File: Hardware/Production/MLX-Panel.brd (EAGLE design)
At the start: 62 x 62 mm, 135 parts, among them U1 MLX90393_MAGNETOMETER, U2 MLX90393_MAGNETOMETER, U3 MLX90393_MAGNETOMETER, U4 MLX90393_MAGNETOMETER, U5 MLX90393_MAGNETOMETER, U6 MLX90393_MAGNETOMETER, U7 MLX90393_MAGNETOMETER, U8 MLX90393_MAGNETOMETER, U9 MLX90393_MAGNETOMETER

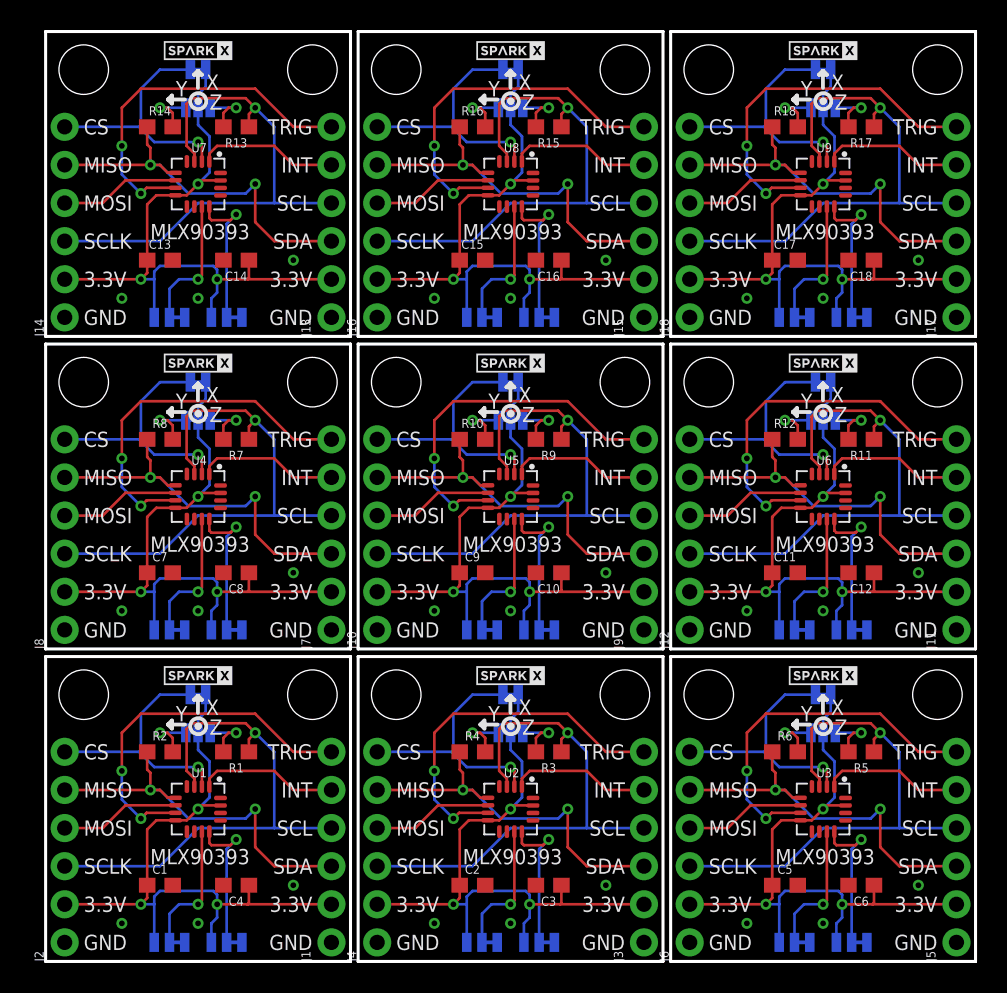
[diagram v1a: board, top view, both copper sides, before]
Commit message: fixed panel with tstop, pushed berbers
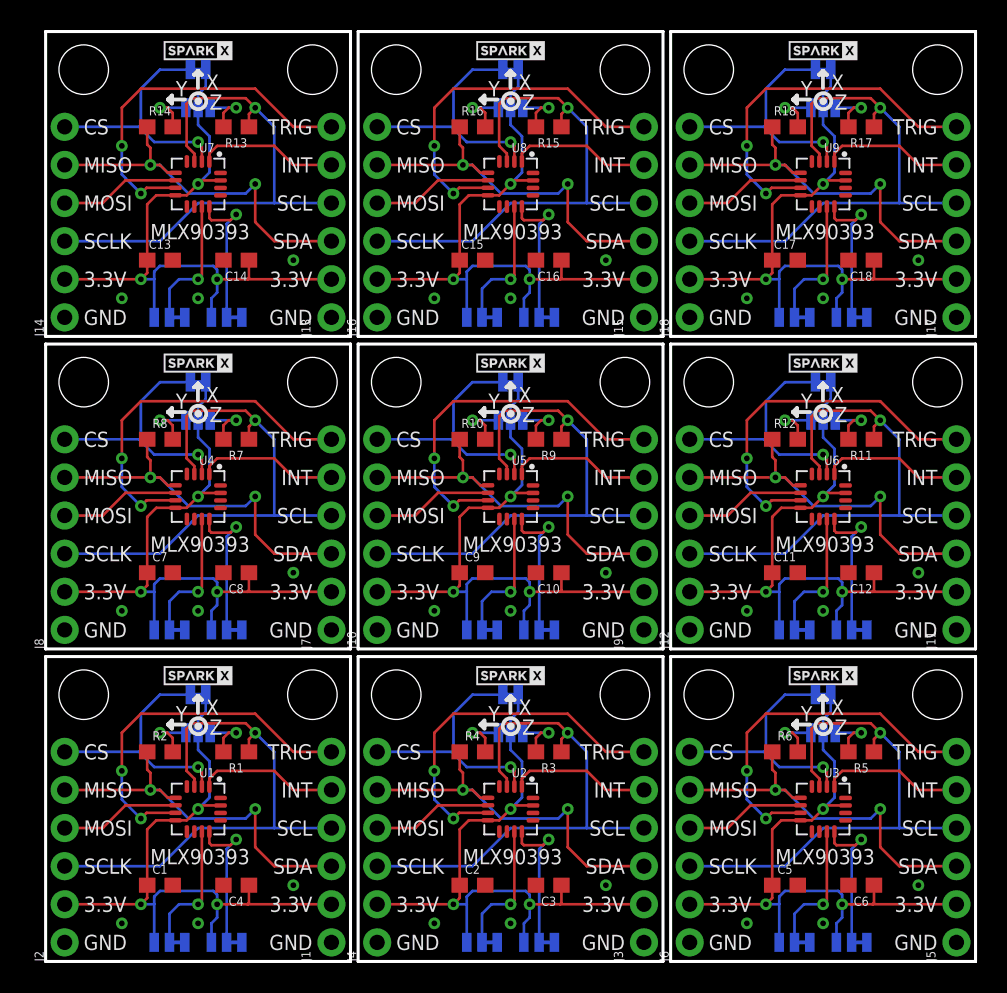
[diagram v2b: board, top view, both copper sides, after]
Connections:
- net GND10 renamed GND1
- net GND11 renamed GND2
- net GND12 renamed GND3
- net GND13 renamed GND4
- net GND14 renamed GND5
- net GND15 renamed GND6
- net GND16 renamed GND7
- net GND17 renamed GND8
- net GND9 renamed GND
